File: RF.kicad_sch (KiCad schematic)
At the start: 5 parts, among them U3 E22-900M30S

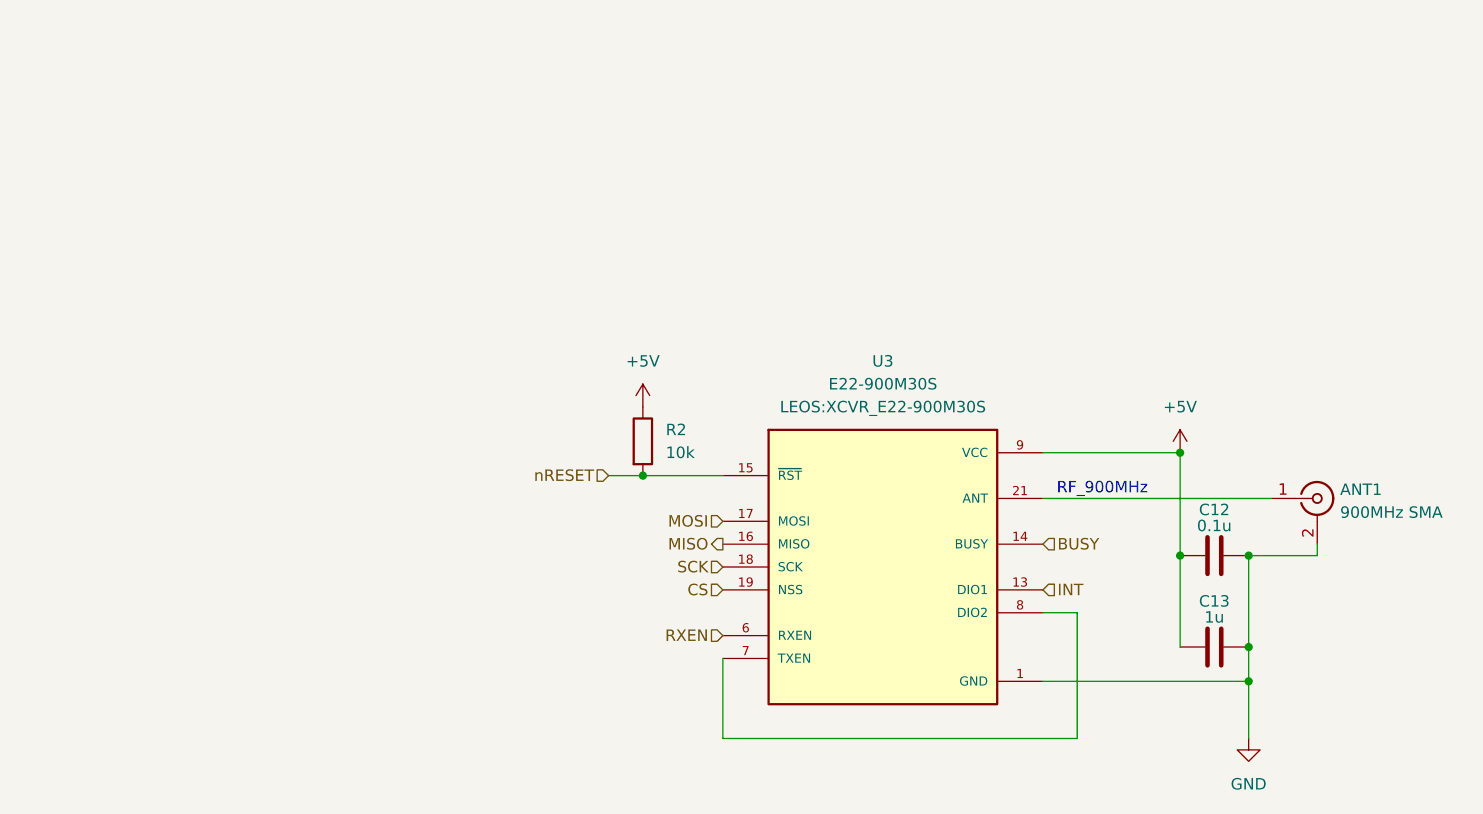
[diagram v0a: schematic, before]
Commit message: Change radio reset pullup to IO voltage, fix net labels
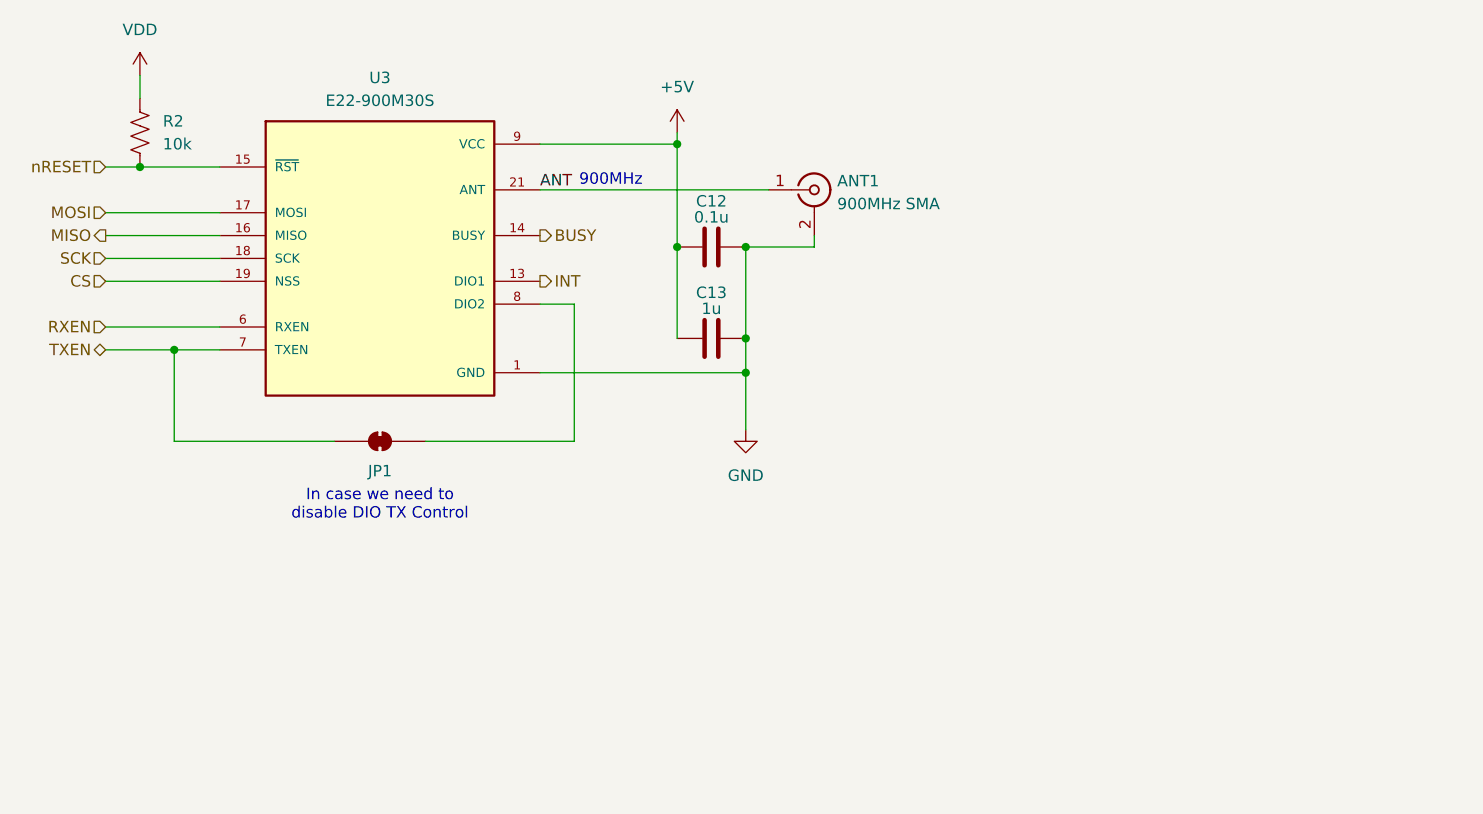
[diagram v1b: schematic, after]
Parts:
- added JP1: SolderJumper_2_Bridged, Jumper:SolderJumper-2_P1.3mm_Bridged_RoundedPad1.0x1.5mm, symbol Jumper:SolderJumper_2_Bridged
- R2: symbol Device:R -> Device:R_US
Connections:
- net +5V: no longer R2.1
- net ANT: now reaches ANT1.1 (In), U3.21 (ANT)
- net at U3.8 (DIO2): now also JP1.2 (B); no longer U3.7 (TXEN)
- new net TXEN: JP1.1 (A), U3.7 (TXEN)
- new net VDD: R2.1
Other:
- note added: "900MHz"
- note added: "In case we need to disable DIO TX Control"
- note removed: "RF_900MHz"
- title: RF -> Ebyte E22-900M30S
- moved on the sheet: ANT1, C12, C13, U3
